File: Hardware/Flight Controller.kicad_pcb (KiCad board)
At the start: 6 copper layers, 40.6 x 40.5 mm, 164 parts, among them J1 USB4110GFA, J10 CAN BUS, J11 CAN BUS, J2 FPV, J3 ST_LINK, J4 GPS, J5 Airspeed sensor, J6 4in1 ESC, J7 RC Receiver, J8 VTX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

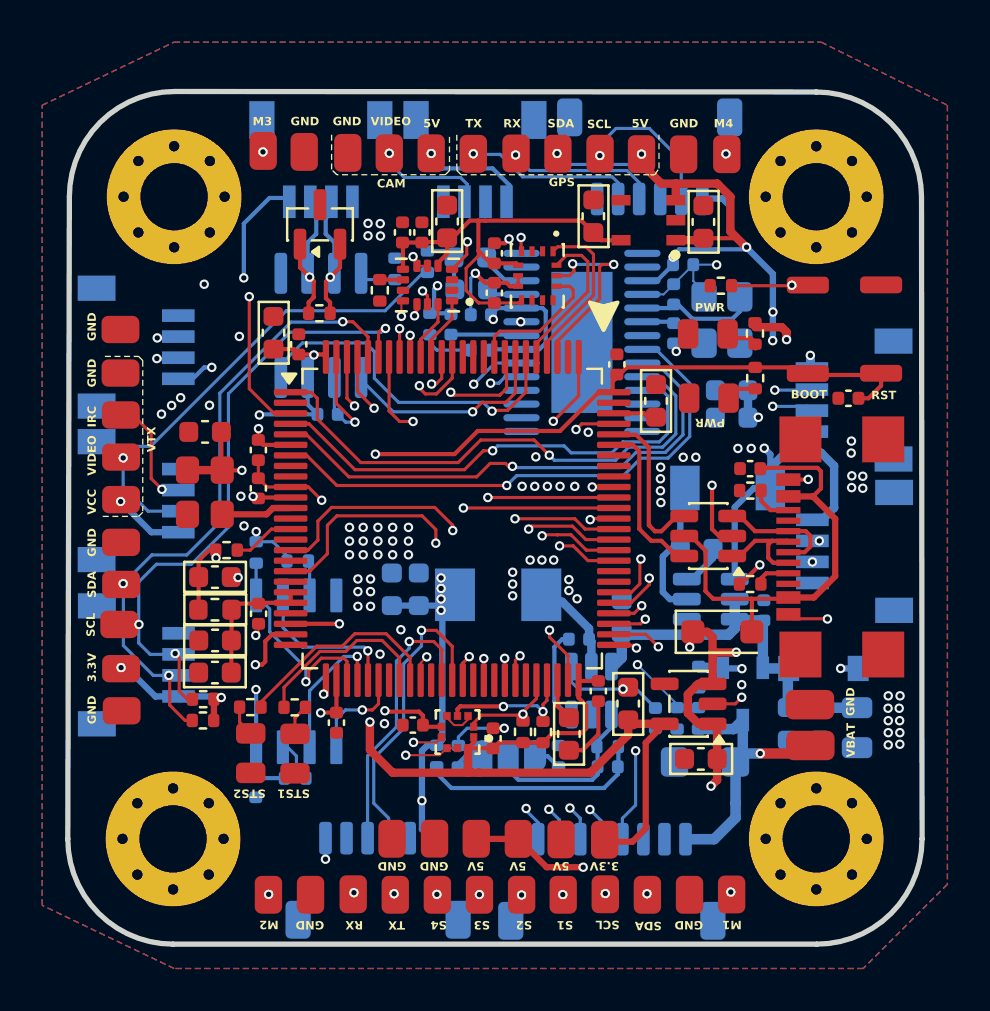
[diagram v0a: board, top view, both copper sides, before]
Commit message: fixed connectors
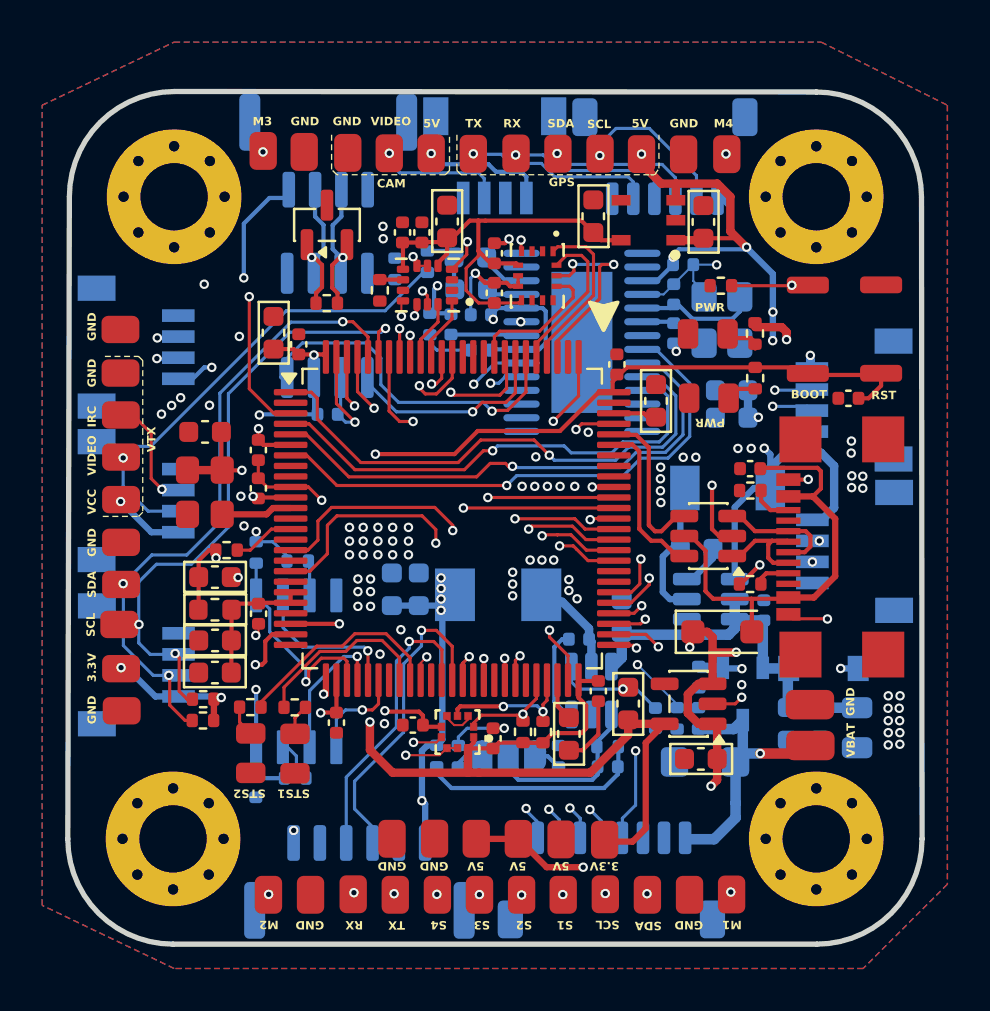
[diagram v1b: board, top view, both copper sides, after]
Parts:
- J10: footprint memo:CONN-SMD_4P-P1.00_SM04B-SRSS-TB-LF-SN -> Connector_JST:JST_GH_SM04B-GHS-TB_1x04-1MP_P1.25mm_Horizontal
- J9: footprint Connector_JST:JST_SH_SM06B-SRSS-TB_1x06-1MP_P1.00mm_Horizontal -> Connector_JST:JST_GH_SM06B-GHS-TB_1x06-1MP_P1.25mm_Horizontal
- moved J2 0.96 mm to (133.5, 80.5)
- moved J9 0.89 mm to (127.1, 114.9)
- moved J4 0.72 mm to (141.6, 80.4)
- moved J10 0.60 mm to (125.6, 80.2)
- moved R28 0.59 mm to (125.5, 87.4)
- moved D8 0.33 mm to (125.5, 83.7)
- moved U14 0.30 mm to (125.5, 88.5)
- moved J6 0.07 mm to (139.0, 114.8)
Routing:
- net DJI_SBUS: track 14.8 -> 13.0 mm
- net CAN_P: track 7.71 -> 6.76 mm
- net GPS_SDA: track 20.6 -> 21.5 mm
- net VIDEO_IN: track 15.2 -> 16.0 mm
- net CAN_N: track 7.58 -> 6.87 mm
- net GPS_TX: track 26.9 -> 27.5 mm
- net DJI_TX: track 14.5 -> 15.2 mm
- net DJI_RX: track 13.3 -> 14.0 mm
- net GND: vias 95 -> 93

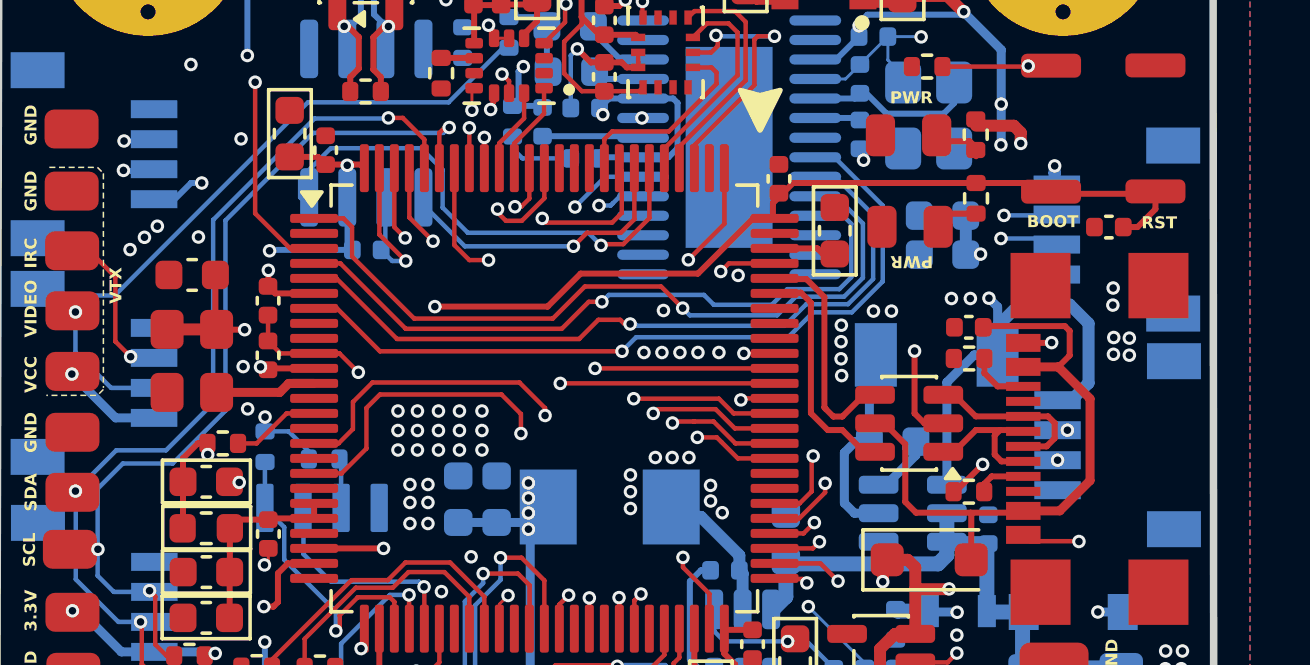
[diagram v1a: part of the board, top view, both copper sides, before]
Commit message: fixed the reset schematics
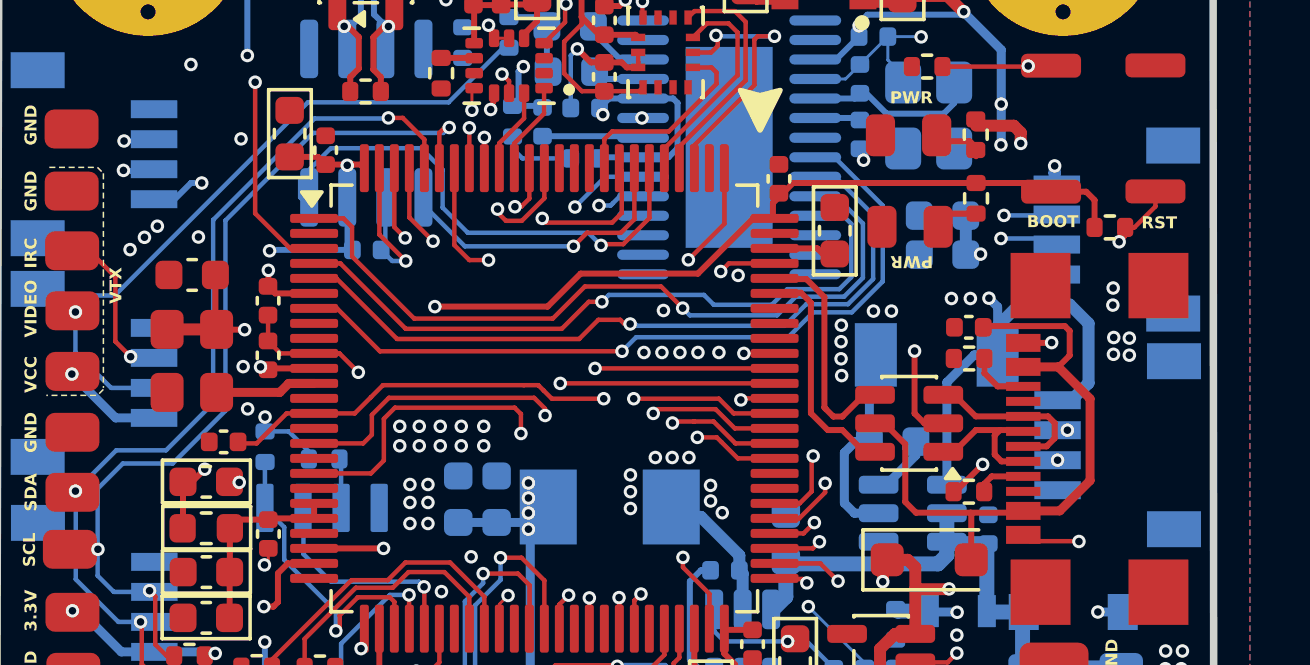
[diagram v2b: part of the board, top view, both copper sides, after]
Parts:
- C9: value 0.1uF -> 4.7uF
- moved R16 30.4 mm to (150.3, 91.9), turned to 180 degrees
- moved C29 30.4 mm to (120.8, 99.1)
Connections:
- C29 pad 2: +3.3V -> NRST
- R16 pad 1: +3.3V -> NRST
- R16 pad 2: NRST -> +3.3V
- SW1 pad 2: +3.3V -> NRST
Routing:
- net NRST: track 2.95 -> 37.0 mm, vias 0 -> 2
- net +3.3V: track 111.8 -> 107.7 mm
- net Net-(U7-PC1): track 26.0 -> 25.4 mm
- net GND: vias 93 -> 88

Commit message: DRC implementation
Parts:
- added G***: LOGO, LOGO, F.Cu at (142.5, 112.7)
- added G***: LOGO, LOGO, B.Cu at (130.7, 95.6)
- moved J10 0.13 mm to (125.6, 80.3)
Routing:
- net NRST: track 37.0 -> 38.4 mm
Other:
- board text added: "Project MANTIS"

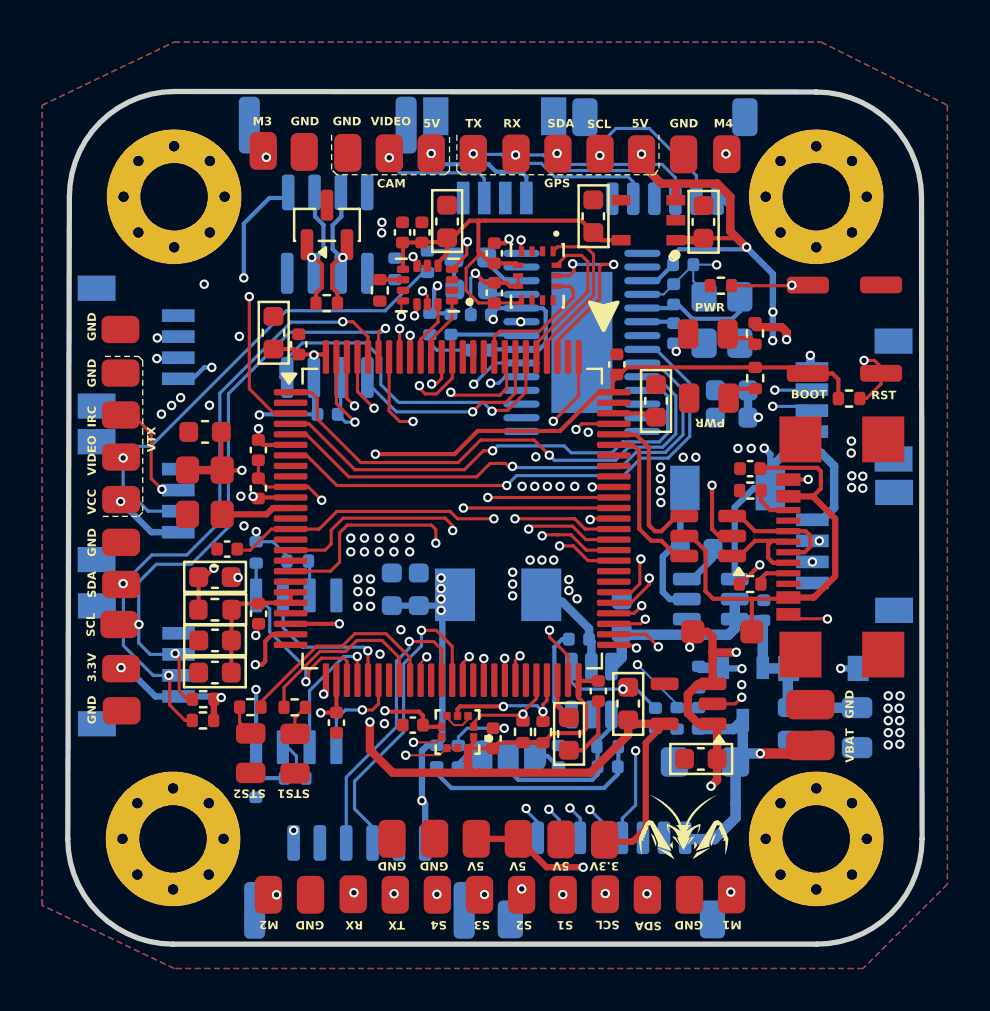
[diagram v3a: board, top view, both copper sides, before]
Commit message: started ground station application
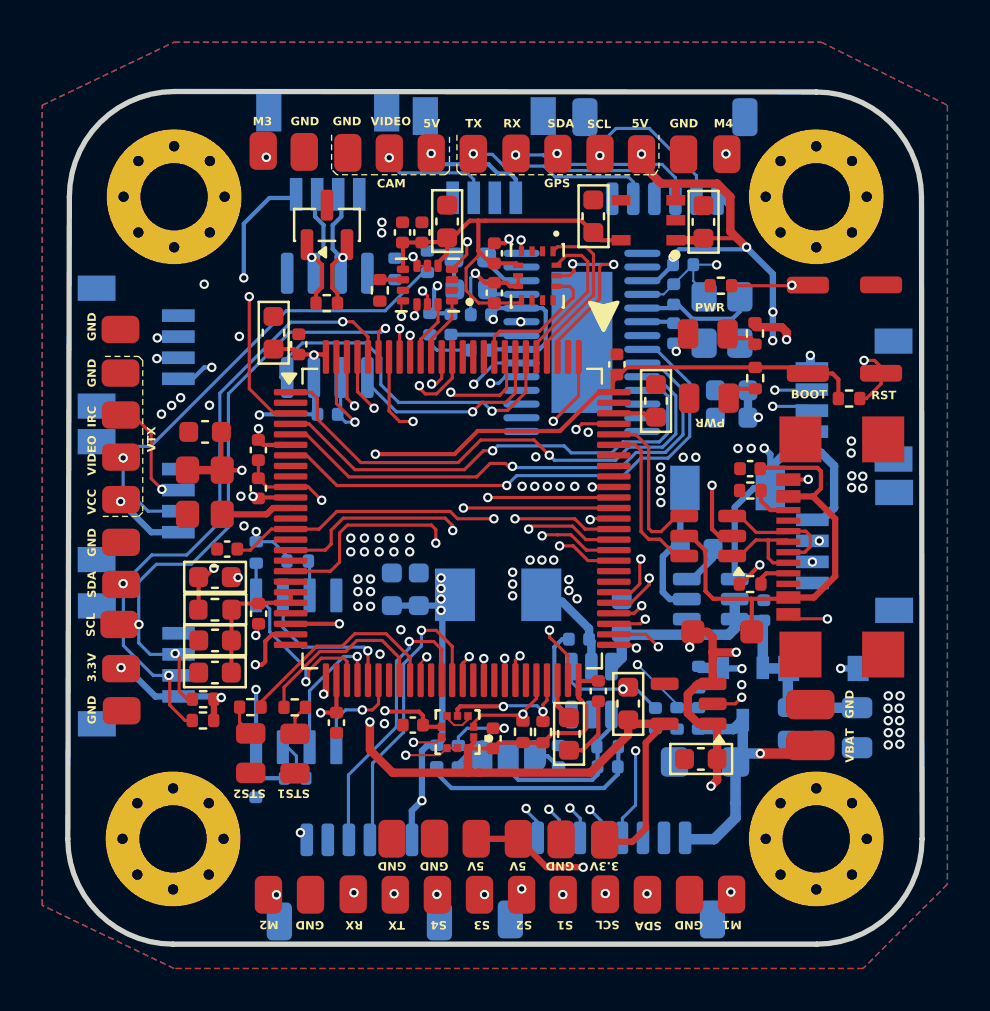
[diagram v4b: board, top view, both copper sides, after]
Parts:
- removed the G*** at (142.5, 112.7)
- removed the G*** at (130.7, 95.6)
- J10: footprint Connector_JST:JST_GH_SM04B-GHS-TB_1x04-1MP_P1.25mm_Horizontal -> memo:CONN-SMD_4P-P1.00_SM04B-SRSS-TB-LF-SN
- J9: footprint Connector_JST:JST_GH_SM06B-GHS-TB_1x06-1MP_P1.25mm_Horizontal -> Connector_JST:JST_SH_SM06B-SRSS-TB_1x06-1MP_P1.00mm_Horizontal
- moved J2 0.50 mm to (133.0, 80.5)
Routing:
- net +3.3V: track 107.7 -> 108.4 mm
- net DJI_TX: track 15.2 -> 14.4 mm
- net +5V: track 111.7 -> 111.1 mm
- net VIDEO_IN: track 15.6 -> 15.1 mm
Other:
- board text added: "CRSF/SBUS"
- board text removed: "Project MANTIS"

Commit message: added quatronion filter, CRSF protocol, and PID loops
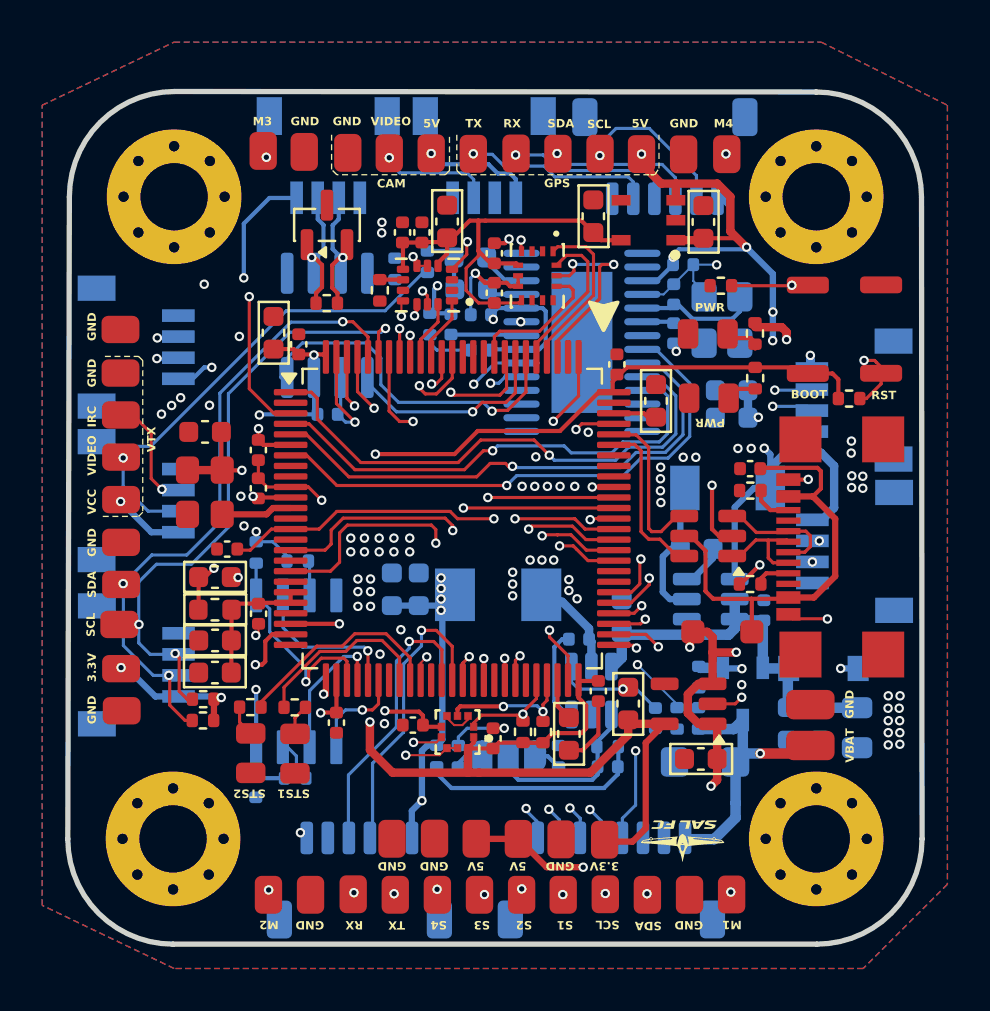
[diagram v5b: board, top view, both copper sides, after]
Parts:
- added G***: LOGO, LOGO, F.Cu at (142.4, 112.7)
- added G***: LOGO, LOGO, B.Cu at (126.9, 95.2)
- moved J10 0.16 mm to (125.6, 80.5)
- moved J9 0.09 mm to (127.1, 114.8)
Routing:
- net CAN_P: track 6.76 -> 5.81 mm
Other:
- board text removed: "CRSF/SBUS"
